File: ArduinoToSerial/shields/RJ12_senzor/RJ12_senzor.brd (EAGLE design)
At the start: 27.6 x 22.9 mm, 2 parts

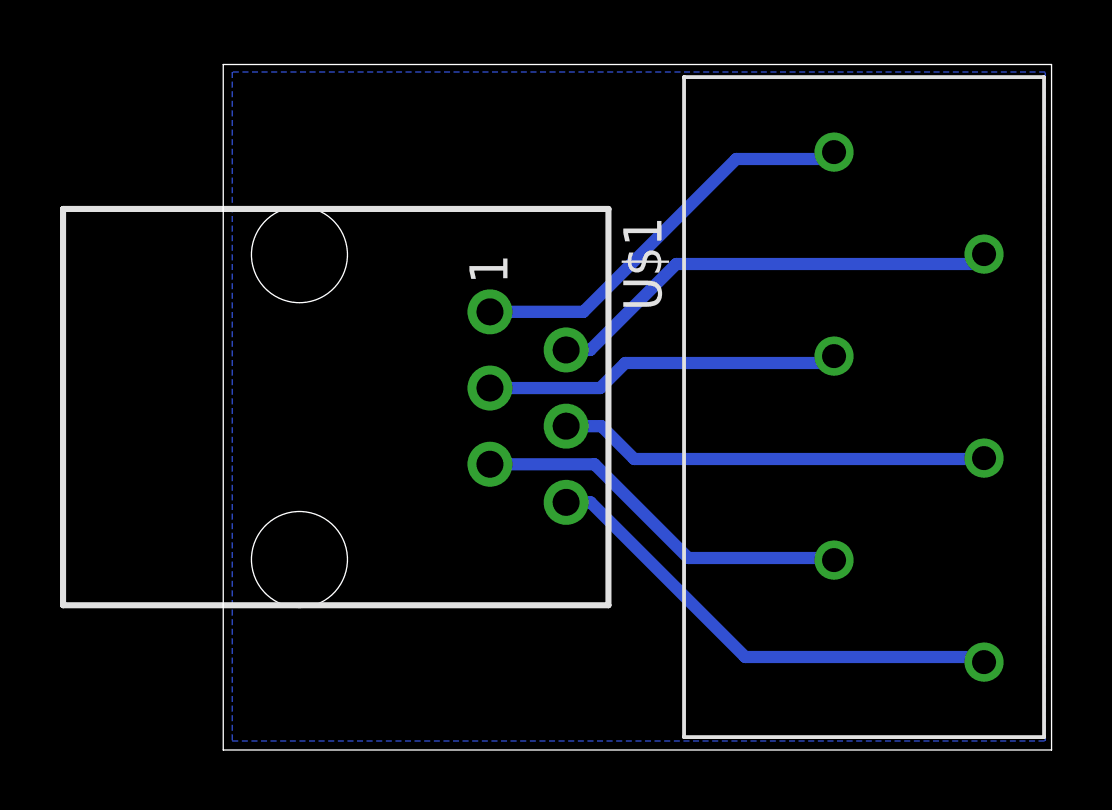
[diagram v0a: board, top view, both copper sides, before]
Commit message: added THT + SMD resistor
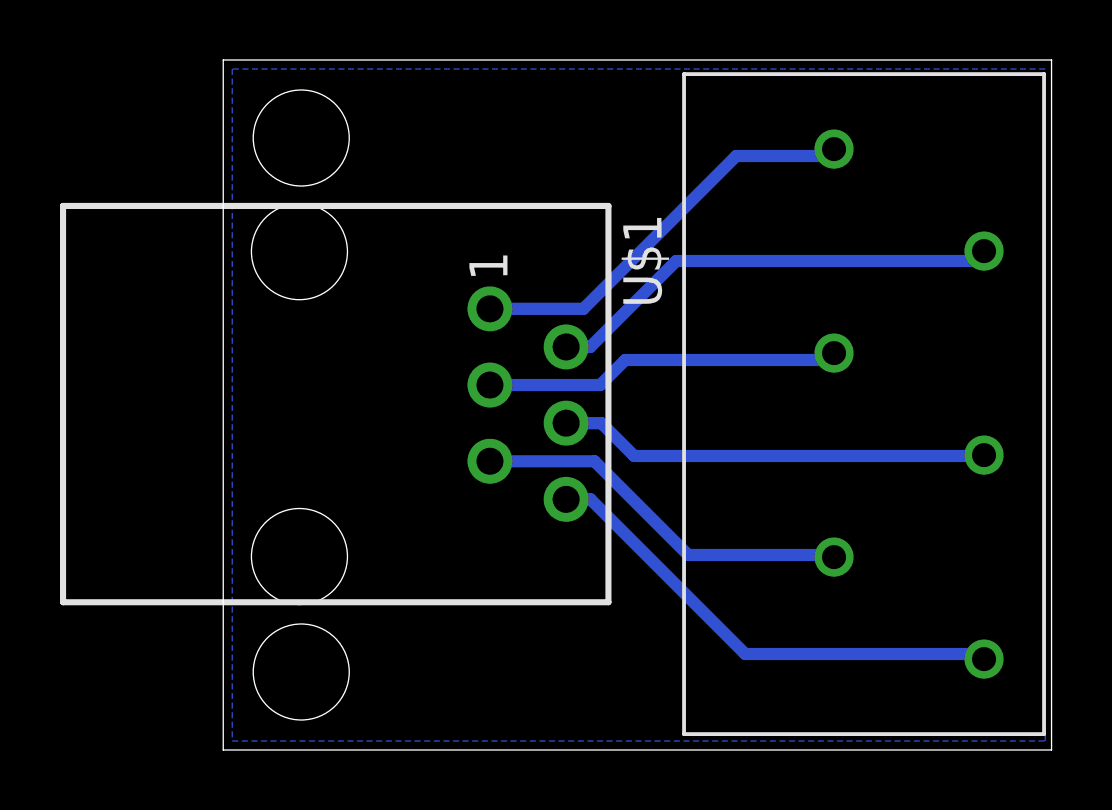
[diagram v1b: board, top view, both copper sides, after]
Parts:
- moved U$1 0.10 mm to (2.54, 11.5)
- moved U$2 0.10 mm to (22.9, 11.5)
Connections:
- removed net N$1: U$1.1, U$2.1
- new net GND: U$1.1, U$2.1
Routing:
- net GND: track 0.00 -> 13.7 mm
- net N$1: track 13.7 -> 0.00 mm
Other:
- board size 27.6 x 22.9 mm -> 27.6 x 23 mm
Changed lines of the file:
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@@
 <layer number="43" name="vRestrict" color="2" fill="10" visible="yes" active="yes"/>
 <layer number="44" name="Drills" color="7" fill="1" visible="no" active="yes"/>
-<layer number="45" name="Holes" color="7" fill="1" visible="no" active="yes"/>
+<layer number="45" name="Holes" color="7" fill="1" visible="yes" active="yes"/>
 <layer number="46" name="Milling" color="3" fill="1" visible="no" active="yes"/>
 <layer number="47" name="Measures" color="7" fill="1" visible="no" active="yes"/>
@@
 <plain>
 <wire x1="0" y1="0" x2="27.61" y2="0" width="0" layer="20"/>
-<wire x1="27.61" y1="0" x2="27.61" y2="22.85" width="0" layer="20"/>
-<wire x1="27.61" y1="22.85" x2="0" y2="22.85" width="0" layer="20"/>
-<wire x1="0" y1="22.85" x2="0" y2="0" width="0" layer="20"/>
+<wire x1="27.61" y1="0" x2="27.61" y2="23" width="0" layer="20"/>
+<wire x1="27.61" y1="23" x2="0" y2="23" width="0" layer="20"/>
+<wire x1="0" y1="23" x2="0" y2="0" width="0" layer="20"/>
+<hole x="2.6" y="20.4" drill="3.2"/>
+<hole x="2.6" y="2.6" drill="3.2"/>
 </plain>
 <attributes>
@@
 </class>
 </classes>
-<designrules name="default">
+<designrules name="default *">
 <description language="de">&lt;b&gt;EAGLE Design Rules&lt;/b&gt;
 &lt;p&gt;
@@
 <param name="mdViaViaSameLayer" value="8mil"/>
 <param name="mnLayersViaInSmd" value="2"/>
-<param name="mdCopperDimension" value="40mil"/>
+<param name="mdCopperDimension" value="0mil"/>
 <param name="mdDrill" value="8mil"/>
 <param name="mdSmdStop" value="0mil"/>
@@
 </autorouter>
 <elements>
-<element name="U$1" library="AtoG" package="RJ12" value="RJ12" x="2.54" y="11.43" rot="R270"/>
-<element name="U$2" library="AtoG" package="CON_SENSOR" value="CON_SENSOR" x="22.86" y="11.43" rot="R270"/>
+<element name="U$1" library="AtoG" package="RJ12" value="RJ12" x="2.54" y="11.53" rot="R270"/>
+<element name="U$2" library="AtoG" package="CON_SENSOR" value="CON_SENSOR" x="22.86" y="11.53" rot="R270"/>
 </elements>
 <signals>
-<signal name="N$1">
-<contactref element="U$1" pad="1"/>
-<contactref element="U$2" pad="1"/>
-<wire x1="8.89" y1="14.605" x2="12.005" y2="14.605" width="0.4064" layer="16"/>
-<wire x1="12.005" y1="14.605" x2="17.1" y2="19.7" width="0.4064" layer="16"/>
-<wire x1="17.1" y1="19.7" x2="20.13" y2="19.7" width="0.4064" layer="16"/>
-<wire x1="20.13" y1="19.7" x2="20.36" y2="19.93" width="0.4064" layer="16"/>
-</signal>
 <signal name="N$2">
 <contactref element="U$1" pad="2"/>
 <contactref element="U$2" pad="2"/>
-<wire x1="11.43" y1="13.335" x2="12.235" y2="13.335" width="0.4064" layer="16"/>
-<wire x1="12.235" y1="13.335" x2="15.1" y2="16.2" width="0.4064" layer="16"/>
-<wire x1="15.1" y1="16.2" x2="25.03" y2="16.2" width="0.4064" layer="16"/>
-<wire x1="25.03" y1="16.2" x2="25.36" y2="16.53" width="0.4064" layer="16"/>
+<wire x1="11.43" y1="13.435" x2="12.235" y2="13.435" width="0.4064" layer="16"/>
+<wire x1="12.235" y1="13.435" x2="15.1" y2="16.3" width="0.4064" layer="16"/>
+<wire x1="15.1" y1="16.3" x2="25.03" y2="16.3" width="0.4064" layer="16"/>
+<wire x1="25.03" y1="16.3" x2="25.36" y2="16.63" width="0.4064" layer="16"/>
 </signal>
 <signal name="N$3">
 <contactref element="U$1" pad="3"/>
 <contactref element="U$2" pad="3"/>
-<wire x1="8.89" y1="12.065" x2="12.565" y2="12.065" width="0.4064" layer="16"/>
-<wire x1="12.565" y1="12.065" x2="13.4" y2="12.9" width="0.4064" layer="16"/>
-<wire x1="13.4" y1="12.9" x2="20.13" y2="12.9" width="0.4064" layer="16"/>
-<wire x1="20.13" y1="12.9" x2="20.36" y2="13.13" width="0.4064" layer="16"/>
+<wire x1="8.89" y1="12.165" x2="12.565" y2="12.165" width="0.4064" layer="16"/>
+<wire x1="12.565" y1="12.165" x2="13.4" y2="13" width="0.4064" layer="16"/>
+<wire x1="13.4" y1="13" x2="20.13" y2="13" width="0.4064" layer="16"/>
+<wire x1="20.13" y1="13" x2="20.36" y2="13.23" width="0.4064" layer="16"/>
 </signal>
 <signal name="N$4">
 <contactref element="U$1" pad="4"/>
 <contactref element="U$2" pad="4"/>
-<wire x1="11.43" y1="10.795" x2="12.605" y2="10.795" width="0.4064" layer="16"/>
-<wire x1="12.605" y1="10.795" x2="13.7" y2="9.7" width="0.4064" layer="16"/>
-<wire x1="13.7" y1="9.7" x2="25.33" y2="9.7" width="0.4064" layer="16"/>
-<wire x1="25.33" y1="9.7" x2="25.36" y2="9.73" width="0.4064" layer="16"/>
+<wire x1="11.43" y1="10.895" x2="12.605" y2="10.895" width="0.4064" layer="16"/>
+<wire x1="12.605" y1="10.895" x2="13.7" y2="9.8" width="0.4064" layer="16"/>
+<wire x1="13.7" y1="9.8" x2="25.33" y2="9.8" width="0.4064" layer="16"/>
+<wire x1="25.33" y1="9.8" x2="25.36" y2="9.83" width="0.4064" layer="16"/>
 </signal>
 <signal name="N$5">
 <contactref element="U$1" pad="5"/>
 <contactref element="U$2" pad="5"/>
-<wire x1="8.89" y1="9.525" x2="12.375" y2="9.525" width="0.4064" layer="16"/>
-<wire x1="12.375" y1="9.525" x2="15.5" y2="6.4" width="0.4064" layer="16"/>
-<wire x1="15.5" y1="6.4" x2="20.29" y2="6.4" width="0.4064" layer="16"/>
-<wire x1="20.29" y1="6.4" x2="20.36" y2="6.33" width="0.4064" layer="16"/>
+<wire x1="8.89" y1="9.625" x2="12.375" y2="9.625" width="0.4064" layer="16"/>
+<wire x1="12.375" y1="9.625" x2="15.5" y2="6.5" width="0.4064" layer="16"/>
+<wire x1="15.5" y1="6.5" x2="20.29" y2="6.5" width="0.4064" layer="16"/>
+<wire x1="20.29" y1="6.5" x2="20.36" y2="6.43" width="0.4064" layer="16"/>
 </signal>
 <signal name="N$6">
 <contactref element="U$1" pad="6"/>
 <contactref element="U$2" pad="6"/>
-<wire x1="11.43" y1="8.255" x2="12.245" y2="8.255" width="0.4064" layer="16"/>
-<wire x1="12.245" y1="8.255" x2="17.4" y2="3.1" width="0.4064" layer="16"/>
-<wire x1="17.4" y1="3.1" x2="25.19" y2="3.1" width="0.4064" layer="16"/>
-<wire x1="25.19" y1="3.1" x2="25.36" y2="2.93" width="0.4064" layer="16"/>
+<wire x1="11.43" y1="8.355" x2="12.245" y2="8.355" width="0.4064" layer="16"/>
+<wire x1="12.245" y1="8.355" x2="17.4" y2="3.2" width="0.4064" layer="16"/>
+<wire x1="17.4" y1="3.2" x2="25.19" y2="3.2" width="0.4064" layer="16"/>
+<wire x1="25.19" y1="3.2" x2="25.36" y2="3.03" width="0.4064" layer="16"/>
 </signal>
 <signal name="GND">
 <polygon width="0.4064" layer="16" isolate="0.4064">
-<vertex x="0.3" y="22.6"/>
+<vertex x="0.3" y="22.7"/>
 <vertex x="0.3" y="0.3"/>
 <vertex x="27.4" y="0.3"/>
-<vertex x="27.4" y="22.6"/>
+<vertex x="27.4" y="22.7"/>
 </polygon>
+<contactref element="U$1" pad="1"/>
+<contactref element="U$2" pad="1"/>
+<wire x1="8.89" y1="14.705" x2="12.005" y2="14.705" width="0.4064" layer="16"/>
+<wire x1="12.005" y1="14.705" x2="17.1" y2="19.8" width="0.4064" layer="16"/>
+<wire x1="17.1" y1="19.8" x2="20.13" y2="19.8" width="0.4064" layer="16"/>
+<wire x1="20.13" y1="19.8" x2="20.36" y2="20.03" width="0.4064" layer="16"/>
 </signal>
 </signals>
